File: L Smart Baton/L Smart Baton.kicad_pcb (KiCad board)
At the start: 2 copper layers, 95 x 60 mm, 0 parts

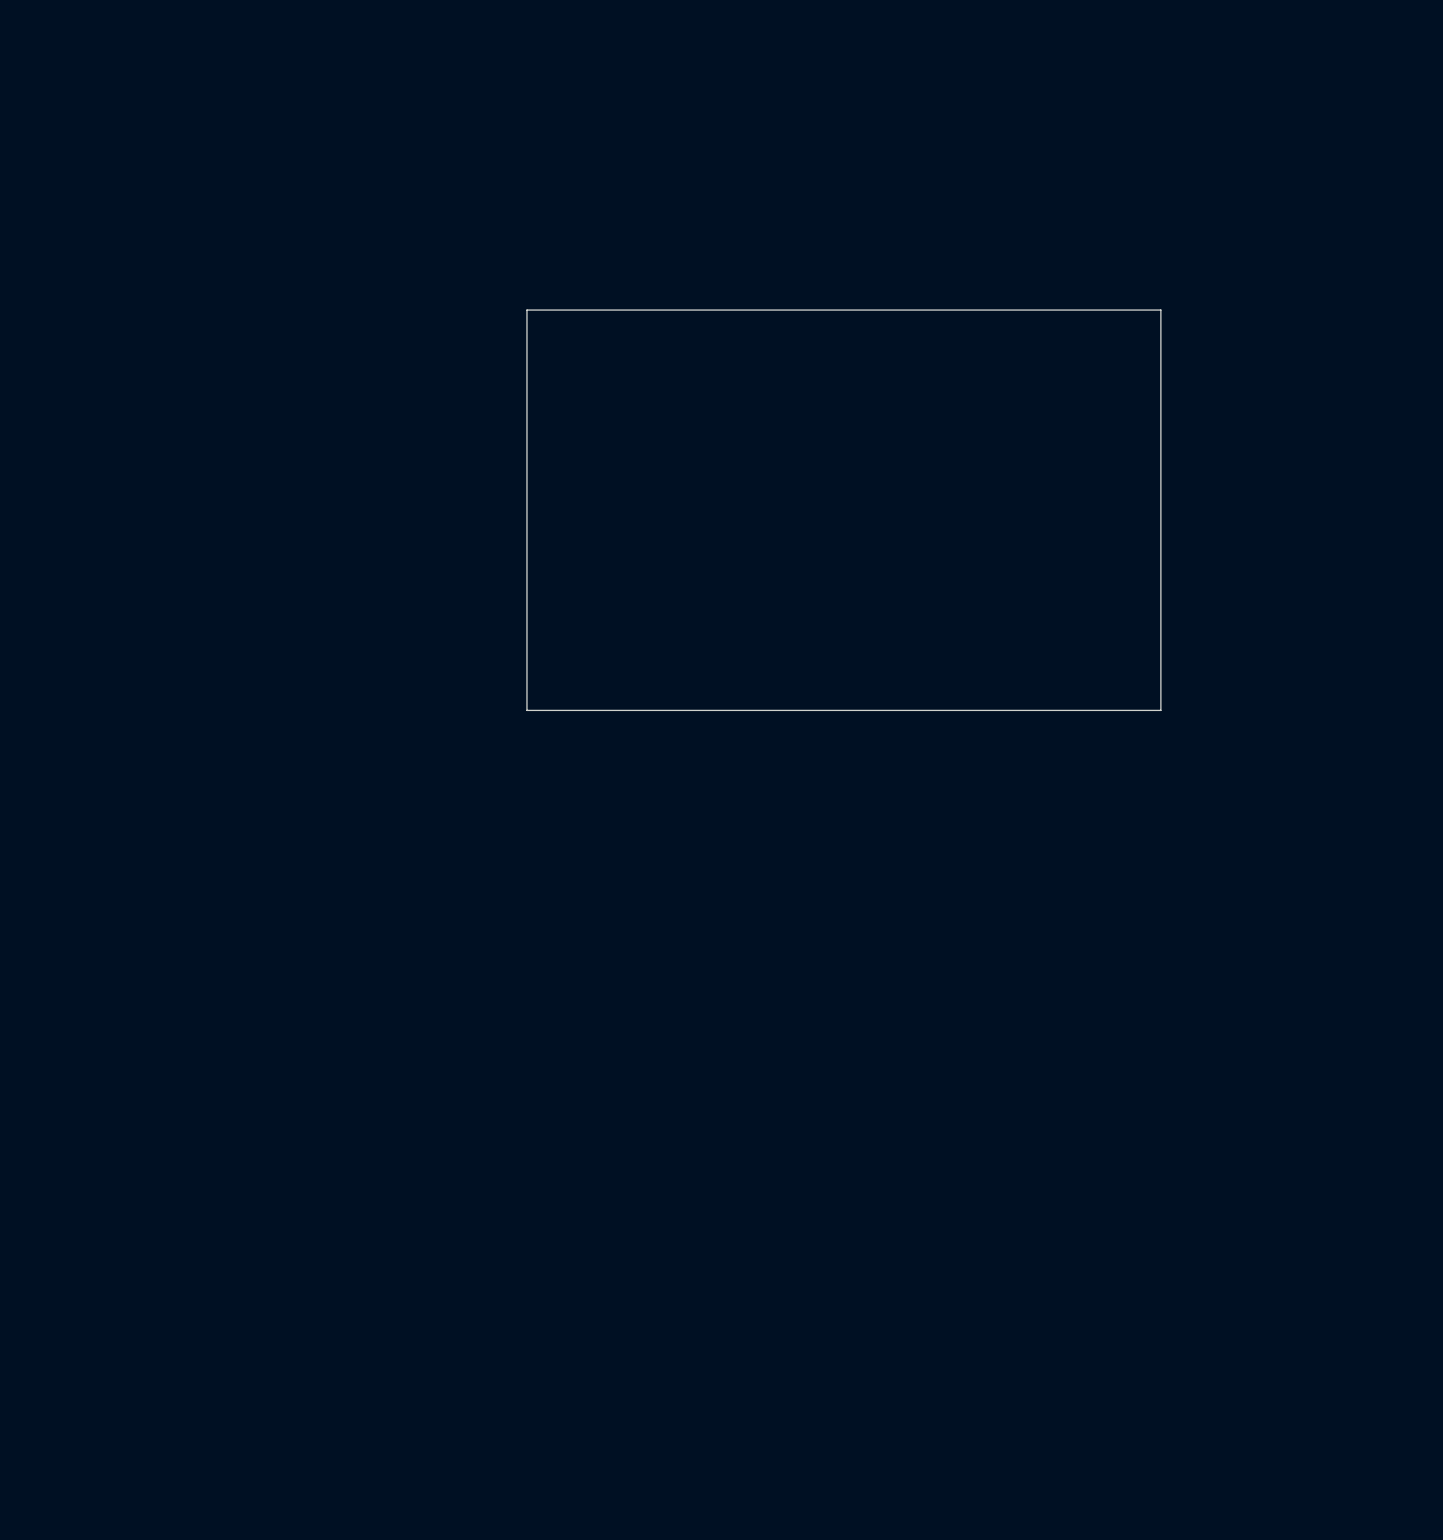
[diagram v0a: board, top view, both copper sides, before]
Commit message: start pcb component placement
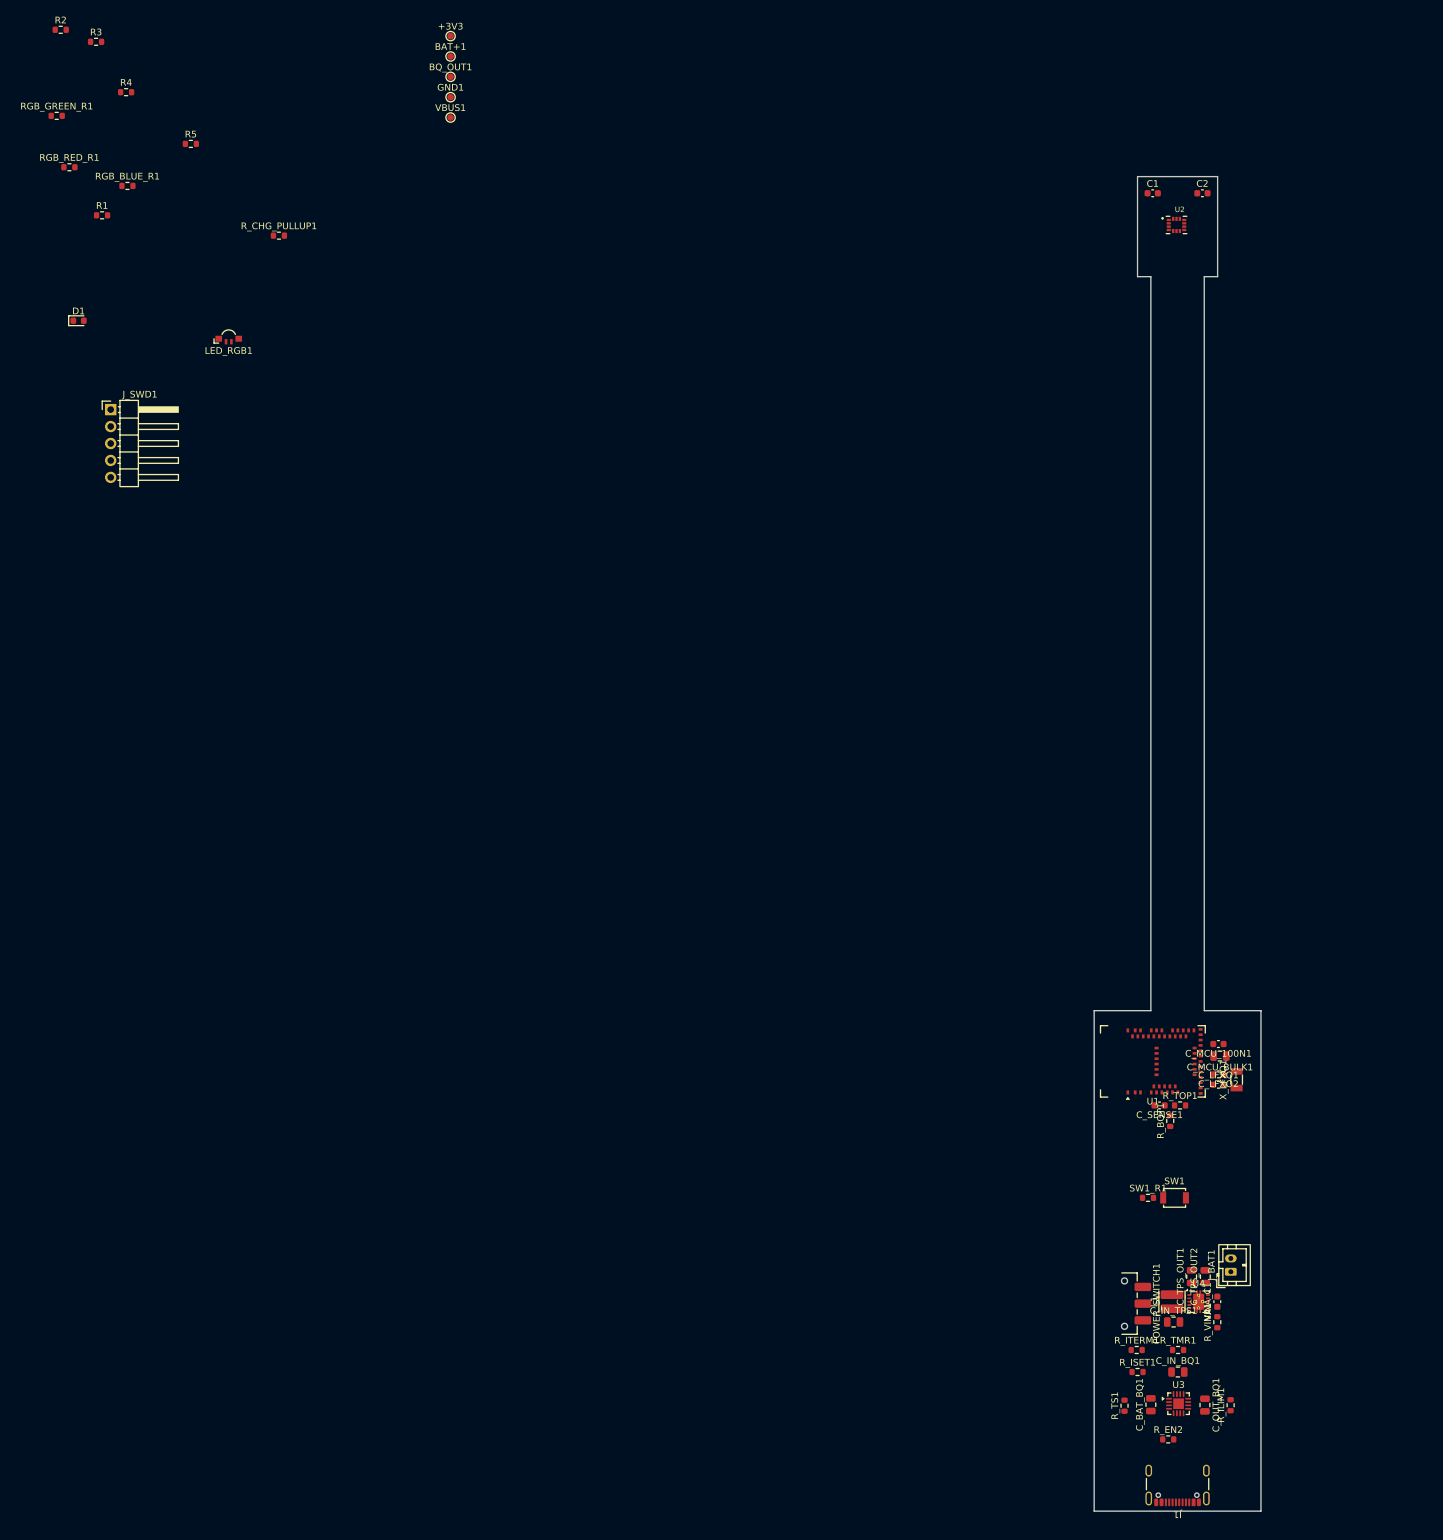
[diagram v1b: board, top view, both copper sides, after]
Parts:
- added +3V3: TestPoint, TestPoint:TestPoint_Pad_D1.0mm, F.Cu at (83.5, 18.9)
- added BAT+1: TestPoint, TestPoint:TestPoint_Pad_D1.0mm, F.Cu at (83.5, 22.0)
- added BQ_OUT1: TestPoint, TestPoint:TestPoint_Pad_D1.0mm, F.Cu at (83.5, 25.1)
- added C1: 100nF, Capacitor_SMD:C_0603_1608Metric, F.Cu at (188.8, 42.5)
- added C2: 100nF, Capacitor_SMD:C_0603_1608Metric, F.Cu at (196.2, 42.5)
- added C_BAT_BQ1: 10uF 10V X7R, Capacitor_SMD:C_0805_2012Metric, F.Cu at (188.5, 224.1)
- added C_IN_BQ1: 1uF 25V X7R, Capacitor_SMD:C_0805_2012Metric, F.Cu at (192.6, 219.2)
- added C_IN_TPS1: 10uF 10V X7R, Capacitor_SMD:C_0805_2012Metric, F.Cu at (191.9, 211.7)
- added C_LFXO1: 10pF, Capacitor_SMD:C_0603_1608Metric, F.Cu at (198.6, 176.1)
- added C_LFXO2: 10pF, Capacitor_SMD:C_0603_1608Metric, F.Cu at (198.6, 174.6)
- added C_MCU_100N1: 100nF, Capacitor_SMD:C_0603_1608Metric, F.Cu at (198.6, 170.0)
- added C_MCU_BULK1: 4.7uF, Capacitor_SMD:C_0805_2012Metric, F.Cu at (198.8, 171.8)
- added C_OUT_BQ1: 10uF 10V X7R, Capacitor_SMD:C_0805_2012Metric, F.Cu at (196.6, 224.1)
- added C_SENSE1: 100nF, Capacitor_SMD:C_0603_1608Metric, F.Cu at (189.8, 179.2)
- added C_TPS_OUT1: 22uF 10V X7R, Capacitor_SMD:C_0805_2012Metric, F.Cu at (194.6, 204.9)
- added C_TPS_OUT2: 22uF 10V X7R, Capacitor_SMD:C_0805_2012Metric, F.Cu at (196.7, 204.9)
- added D1: APT1608QBC/D, LED_SMD:LED_0603_1608Metric, F.Cu at (27.8, 61.6)
- added GND1: TestPoint, TestPoint:TestPoint_Pad_D1.0mm, F.Cu at (83.5, 28.1)
- added J1: USB4105-GF-A, Connector_USB:USB_C_Receptacle_GCT_USB4105-xx-A_16P_TopMnt_Horizontal, F.Cu at (192.5, 235.0)
- added J_BAT1: Conn_01x02, Connector_JST:JST_PH_B2B-PH-K_1x02_P2.00mm_Vertical, F.Cu at (200.5, 204.1)
- added J_SWD1: 22052051, Connector_PinHeader_2.54mm:PinHeader_1x05_P2.54mm_Horizontal, F.Cu at (32.6, 74.9)
- added L1: 74438335022, Inductor_SMD:L_Wuerth_MAPI-3015, F.Cu at (191.7, 208.6)
- added LED_RGB1: APFA3010LSEEZGKQBKC, LED_SMD:LED_Kingbright_APFA3010_3x1.5mm_Horizontal, F.Cu at (50.3, 64.3)
- added POWER_SWITCH1: JS102011SAQN, Button_Switch_SMD:SW_SPDT_CK_JS102011SAQN, F.Cu at (184.6, 208.9)
- added R1: 4.7k, Resistor_SMD:R_0603_1608Metric, F.Cu at (31.3, 45.8)
- added R2: 4.7k, Resistor_SMD:R_0603_1608Metric, F.Cu at (25.1, 18.0)
- added R3: 330, Resistor_SMD:R_0603_1608Metric, F.Cu at (30.4, 19.8)
- added R4: 5.1k, Resistor_SMD:R_0603_1608Metric, F.Cu at (34.9, 27.4)
- added R5: 5.1k, Resistor_SMD:R_0603_1608Metric, F.Cu at (44.6, 35.1)
- added RGB_BLUE_R1: 330, Resistor_SMD:R_0603_1608Metric, F.Cu at (35.1, 41.4)
- added RGB_GREEN_R1: 330, Resistor_SMD:R_0603_1608Metric, F.Cu at (24.5, 30.9)
- added RGB_RED_R1: 750, Resistor_SMD:R_0603_1608Metric, F.Cu at (26.4, 38.6)
- added R_BOT1: 1M, Resistor_SMD:R_0603_1608Metric, F.Cu at (191.4, 181.5)
- added R_CHG_PULLUP1: 10k, Resistor_SMD:R_0603_1608Metric, F.Cu at (57.8, 48.9)
- added R_EN2: 10k, Resistor_SMD:R_0603_1608Metric, F.Cu at (191.1, 229.2)
- added R_ILIM1: 3.09k, Resistor_SMD:R_0603_1608Metric, F.Cu at (200.4, 224.1)
- added R_ISET1: 3.57k, Resistor_SMD:R_0603_1608Metric, F.Cu at (186.5, 219.2)
- added R_ITERM1: 3k, Resistor_SMD:R_0603_1608Metric, F.Cu at (186.4, 215.8)
- added R_TMR1: 46.4k, Resistor_SMD:R_0603_1608Metric, F.Cu at (192.6, 215.8)
- added R_TOP1: 1M, Resistor_SMD:R_0603_1608Metric, F.Cu at (192.9, 179.2)
- added R_TS1: 10k, Resistor_SMD:R_0603_1608Metric, F.Cu at (184.6, 224.2)
- added R_VINA1: 100, Resistor_SMD:R_0603_1608Metric, F.Cu at (198.5, 211.7)
- added SW1: B3U-1000P, Button_Switch_SMD:SW_SPST_B3U-1000P, F.Cu at (192.1, 193.1)
- added SW1_R1: 1k, Resistor_SMD:R_0603_1608Metric, F.Cu at (188.1, 193.1)
- added U1: MDBT50Q-1MV2, RF_Module:Raytac_MDBT50Q, F.Cu at (188.8, 172.6)
- added U2: LSM6DSOX, LSM6DSOX:PQFN50P250X300X86-14N, F.Cu at (192.3, 47.2)
- added U3: BQ24074RGT, Package_DFN_QFN:VQFN-16-1EP_3x3mm_P0.5mm_EP1.6x1.6mm, F.Cu at (192.7, 223.9)
- added U4: TPS63001, Package_SON:Texas_DRC0010J_ThermalVias, F.Cu at (195.7, 208.6)
- added VBUS1: TestPoint, TestPoint:TestPoint_Pad_D1.0mm, F.Cu at (83.5, 31.1)
- added VINA_C1: 0.1uF, Capacitor_SMD:C_0603_1608Metric, F.Cu at (198.5, 208.6)
- added X_LFXO1: FC-135 32.768kHz 7pF, Crystal:Crystal_SMD_3215-2Pin_3.2x1.5mm, F.Cu at (201.3, 175.3)
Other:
- board size 95 x 60 mm -> 25 x 200 mm
- board text removed: "KiCad footprint merge request screenshot template (large parts)"
- board text removed: "This template is for quickly creating diagrams for KiCad symbols and footprints. Steps to create a helpful screenshot for a merge request: * Add the new or modified footprint to this PCB layout * Use the dimension tool to create a full-specified dimensioned drawing of the footprint * Take a screenshot of the footprint and insert it into the GitLab merge request description field * Optionally, set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"

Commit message: Add files via upload
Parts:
- moved R3 276.1 mm to (201.5, 236.5)
- moved RGB_GREEN_R1 258.4 mm to (182.0, 235.8), turned to 90 degrees
- moved R4 256.0 mm to (191.5, 229.8), turned to 90 degrees
- moved RGB_RED_R1 253.7 mm to (186.0, 235.8), turned to 90 degrees
- moved D1 247.9 mm to (201.5, 238.5)
- moved R5 246.5 mm to (194.8, 230.6)
- moved RGB_BLUE_R1 244.9 mm to (184.0, 235.8), turned to 90 degrees
- moved R2 236.7 mm to (196.2, 181.5), turned to -90 degrees
- moved GND1 233.0 mm to (199.0, 230.5)
- moved R_CHG_PULLUP1 225.0 mm to (194.0, 228.0), turned to 90 degrees
- moved BAT+1 224.3 mm to (187.0, 221.0)
- moved VBUS1 222.2 mm to (187.5, 227.5)
- moved LED_RGB1 219.3 mm to (183.5, 238.5), turned to 180 degrees
- moved R1 212.4 mm to (194.7, 181.5), turned to 90 degrees
- moved BQ_OUT1 208.9 mm to (188.0, 206.0)
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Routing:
- net +3V3: track 0.00 -> 254.7 mm, vias 0 -> 17
- net GND: track 0.00 -> 225.6 mm, vias 0 -> 25
- net Net-(U1-P0.26): track 0.00 -> 147.9 mm, vias 0 -> 5
- net Net-(U1-P0.27): track 0.00 -> 146.7 mm, vias 0 -> 6
- net /IMU_INT2: track 0.00 -> 122.7 mm, vias 0 -> 4
- net /IMU_INT1: track 0.00 -> 120.4 mm
- net /BLE_LED: track 0.00 -> 86.0 mm, vias 0 -> 4
- net /CHG_STATUS: track 0.00 -> 79.1 mm, vias 0 -> 7
- net /RGB_RED: track 0.00 -> 76.1 mm, vias 0 -> 4
- net /RGB_BLUE: track 0.00 -> 71.6 mm, vias 0 -> 2
- net /RGB_GREEN: track 0.00 -> 69.5 mm, vias 0 -> 2
- net Net-(J_BAT1-Pin_1): track 0.00 -> 61.6 mm, vias 0 -> 6
- net /SWDCLK: track 0.00 -> 40.6 mm, vias 0 -> 7
- net Net-(U3-IN): track 0.00 -> 40.6 mm, vias 0 -> 5
- net /SW_POW: track 0.00 -> 39.8 mm, vias 0 -> 4
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- added copper zone on B.Cu, net GND

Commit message: ALMOST FINAL
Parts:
- added REF**: MountingHole_2.1mm, MountingHole:MountingHole_2.1mm, F.Cu at (210.0, 148.5)
- added REF**: MountingHole_2.1mm, MountingHole:MountingHole_2.1mm, F.Cu at (218.6, 178.4)
- added REF**: MountingHole_2.1mm, MountingHole:MountingHole_2.1mm, F.Cu at (201.4, 178.4)
- moved BAT+1 71.1 mm to (220.0, 158.0)
- moved GND1 68.3 mm to (220.0, 165.5)
- moved VBUS1 67.8 mm to (220.0, 168.0)
- moved BQ_OUT1 55.6 mm to (220.0, 160.5)
- moved POWER_SWITCH1 53.8 mm to (201.0, 152.0)
- moved J_BAT1 53.6 mm to (217.9, 152.5)
- moved C_BAT_BQ1 53.4 mm to (206.0, 173.4)
- moved C_IN_BQ1 53.4 mm to (210.0, 168.4)
- moved C_OUT_BQ1 53.4 mm to (214.0, 173.4)
- moved J1 53.4 mm to (210.0, 186.0)
- moved LED_RGB1 53.4 mm to (201.0, 188.0)
- moved R4 53.4 mm to (209.0, 179.3)
- moved R5 53.4 mm to (212.2, 180.1)
- moved RGB_BLUE_R1 53.4 mm to (201.5, 185.3)
- moved RGB_GREEN_R1 53.4 mm to (199.5, 185.3)
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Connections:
- U1 pad 22: unconnected-(U1-P0.06-Pad22) -> /BLE_LED
- U1 pad 43: /BLE_LED -> unconnected-(U1-P0.21-Pad43)
- U1 pad 46: /RGB_RED -> unconnected-(U1-P0.22-Pad46)
- U1 pad 47: unconnected-(U1-P1.00-Pad47) -> /RGB_RED
- U1 pad 48: /RGB_BLUE -> unconnected-(U1-P0.24-Pad48)
- U1 pad 49: unconnected-(U1-P0.25-Pad49) -> /RGB_BLUE
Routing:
- net GND: track 225.6 -> 26.1 mm, vias 25 -> 12
- net /IMU_INT1: track 120.4 -> 57.2 mm
- net /IMU_INT2: track 122.7 -> 60.3 mm, vias 4 -> 2
- net Net-(U1-P0.27): track 146.7 -> 92.2 mm, vias 6 -> 2
- net Net-(U1-P0.26): track 147.9 -> 94.8 mm, vias 5 -> 0
- net +3V3: track 254.7 -> 221.6 mm, vias 17 -> 13
- net /CHG_STATUS: track 79.1 -> 62.0 mm, vias 7 -> 4
- net Net-(POWER_SWITCH1-A): track 23.7 -> 40.5 mm, vias 4 -> 0
- net /BLE_LED: track 86.0 -> 70.0 mm, vias 4 -> 2
- net /USER_BTN: track 36.0 -> 21.2 mm, vias 4 -> 0
- net /SWDCLK: track 40.6 -> 27.1 mm, vias 7 -> 1
- net /SW_POW: track 39.8 -> 52.1 mm
- net /RGB_RED: track 76.1 -> 66.5 mm, vias 4 -> 2
- net /SWDIO: track 35.4 -> 26.4 mm, vias 3 -> 1
- net Net-(U3-IN): track 40.6 -> 35.3 mm, vias 5 -> 6
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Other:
- board size 25 x 200 mm -> 23 x 130 mm
